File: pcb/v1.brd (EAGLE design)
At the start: 92 x 80 mm, 54 parts, among them U2 MMBT3904, U3 MMBT3904, U4 MMBT3904, U5 MMBT3904

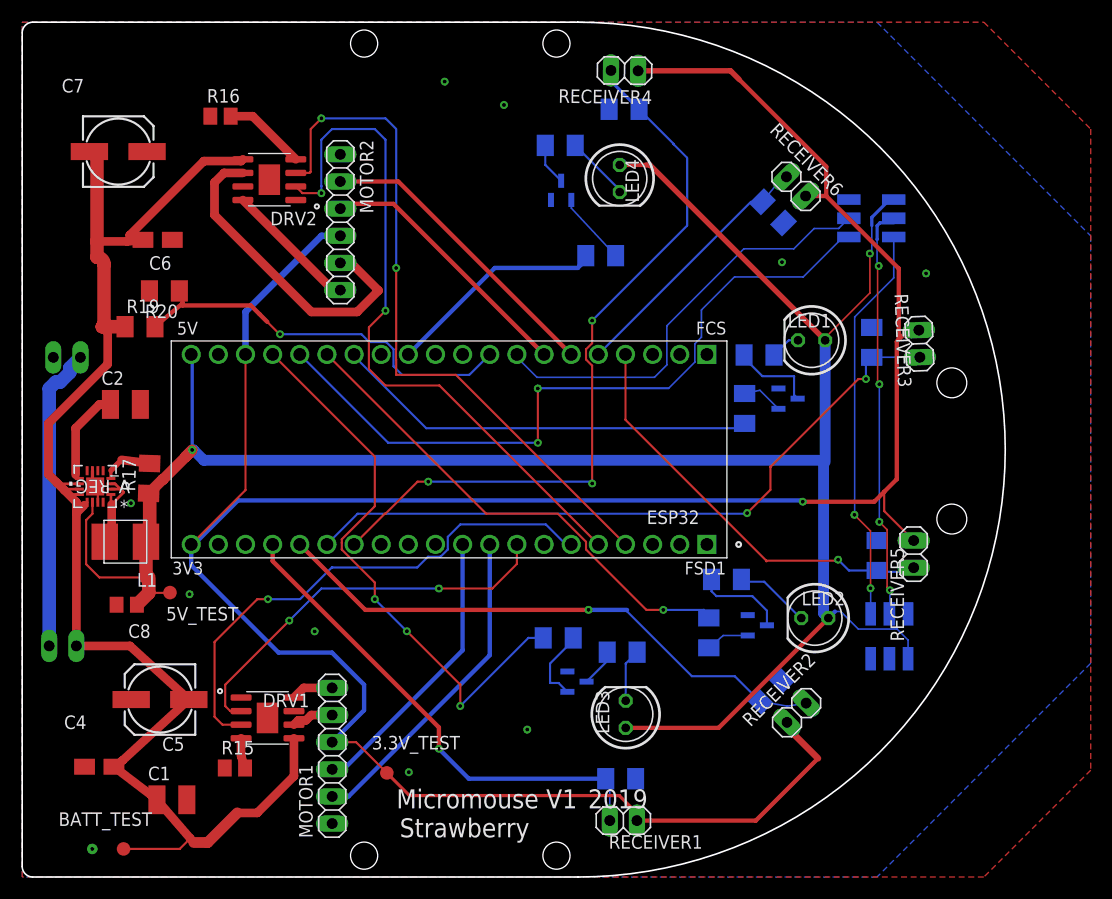
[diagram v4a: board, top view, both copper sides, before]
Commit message: Changed pin placement
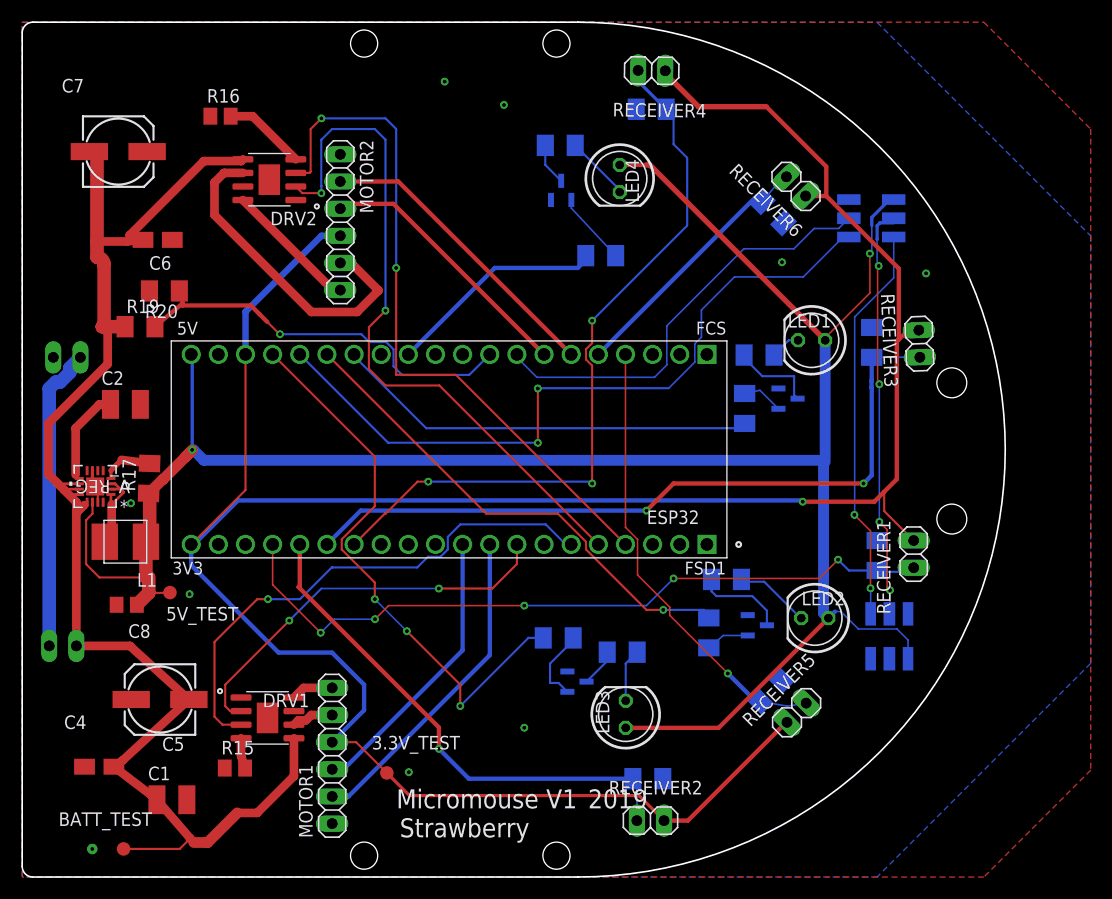
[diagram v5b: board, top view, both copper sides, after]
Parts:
- moved RECEIVER1 36.9 mm to (83.4, 30.2), turned to 270 degrees
- moved RECEIVER5 18.4 mm to (72.5, 15.4), turned to 45 degrees
- moved RECEIVER2 17.0 mm to (58.8, 5.28), turned to 180 degrees
- moved R12 2.54 mm to (58.9, 71.9)
- moved R9 2.54 mm to (58.5, 9.20)
- moved RECEIVER4 2.54 mm to (58.9, 75.5)
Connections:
- net REC1: now also R13.2; no longer R9.2
- net REC2: now also R9.2; no longer R10.2
- net REC5: now also R10.2; no longer R13.2
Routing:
- net REC1: track 46.4 -> 69.2 mm, vias 1 -> 5
- net 3.3V: track 253.0 -> 244.1 mm
- net REC2: track 53.6 -> 48.0 mm
- net REC3: track 64.9 -> 69.2 mm
- net REC5: track 39.3 -> 43.1 mm
- net REC4: track 70.6 -> 69.5 mm
- net REC6: track 24.6 -> 25.2 mm

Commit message: Flipped the back sensor resistors
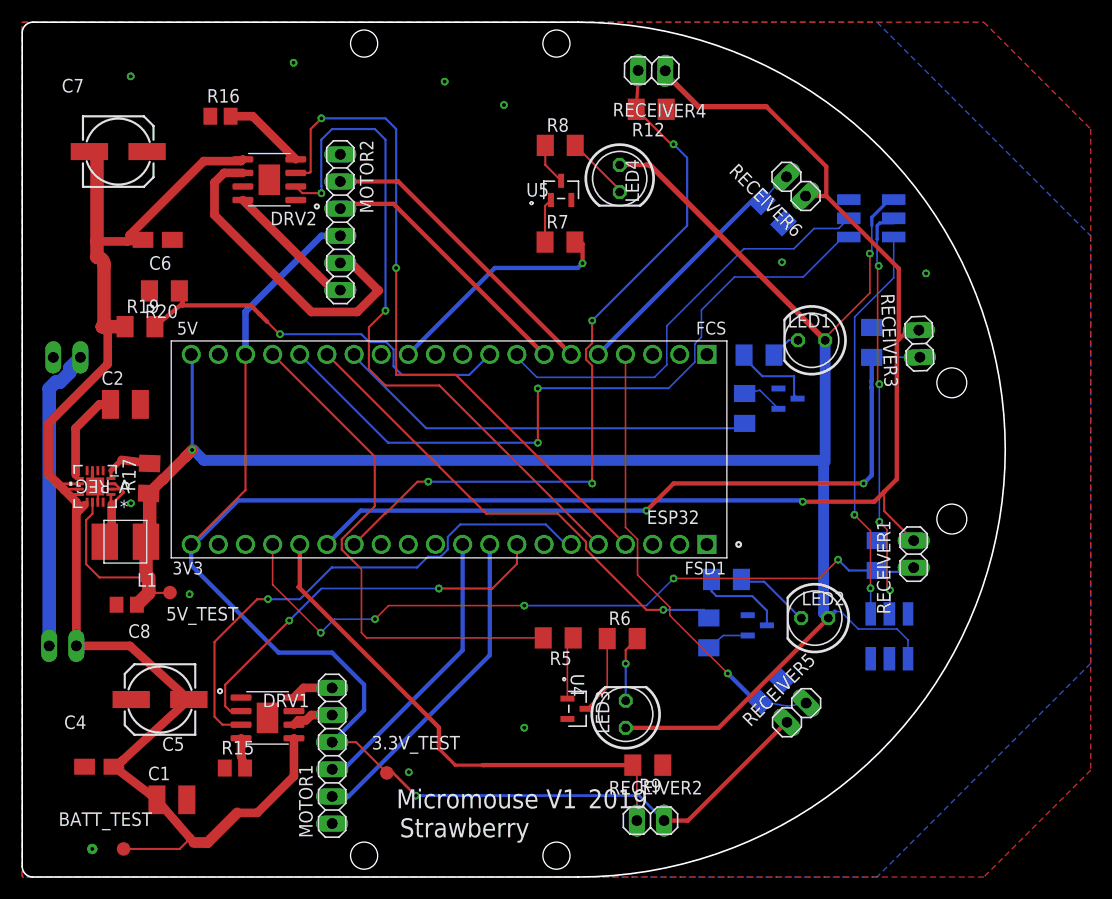
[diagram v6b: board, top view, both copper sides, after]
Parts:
- moved R7 4.02 mm to (50.3, 59.4), flipped to the top
- moved U4 2.54 mm to (52.0, 15.7), flipped to the top, turned to 270 degrees
- moved R6 1.27 mm to (56.2, 22.3), flipped to the top, turned to 0 degrees
- moved R9 1.27 mm to (58.5, 10.5), flipped to the top, turned to 180 degrees
- flipped R12 to the top
- flipped R5 to the top, turned to 180 degrees
- flipped R8 to the top, turned to 0 degrees
- flipped U5 to the top
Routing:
- net N$12: track 3.56 -> 7.47 mm
- net EM3: track 53.2 -> 49.3 mm, vias 3 -> 0
- net N$13: track 6.85 -> 4.18 mm
- net EM4: track 20.6 -> 22.4 mm, vias 0 -> 1
- net N$11: track 4.99 -> 6.26 mm, vias 0 -> 1
- net N$10: track 7.08 -> 5.91 mm
- net 5V: track 205.4 -> 204.3 mm
- net REC2: track 48.0 -> 48.9 mm, vias 1 -> 0
- net REC4: track 69.5 -> 69.7 mm, vias 3 -> 4
- net 3.3V: vias 1 -> 2

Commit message: Evened out the holes to make pcb look nicer
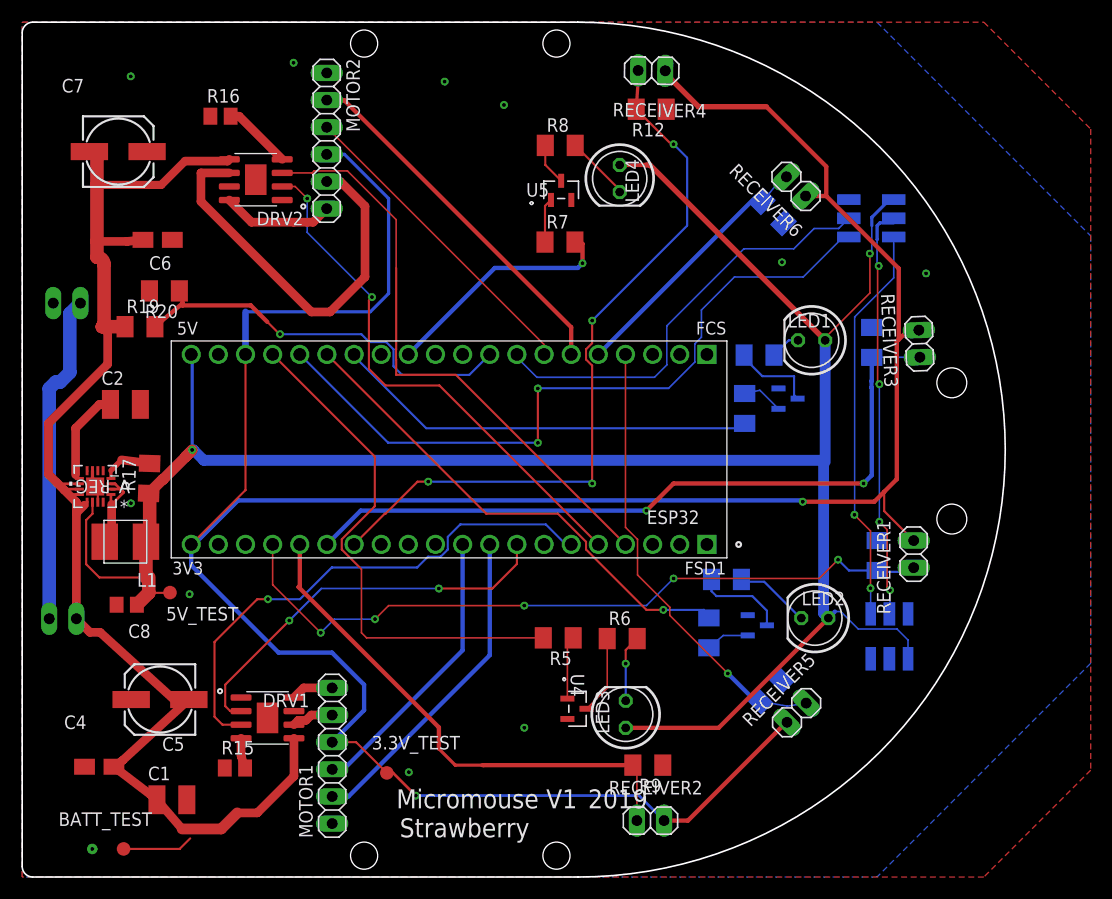
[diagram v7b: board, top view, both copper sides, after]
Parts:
- moved MOTOR2 7.73 mm to (28.5, 68.9)
- moved BATT2 5.08 mm to (4.18, 53.7)
- moved BATT1 2.54 mm to (3.80, 24.2)
- moved DRV2 1.27 mm to (21.9, 65.3)
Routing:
- net 3.3V: track 244.1 -> 262.8 mm
- net PWM1B: track 64.9 -> 49.7 mm
- net PWM1A: track 65.3 -> 55.2 mm, vias 2 -> 0
- net N$19: track 30.7 -> 37.5 mm
- net EN1A: track 28.3 -> 34.2 mm
- net EN1B: track 25.1 -> 29.7 mm
- net BATT_POWER: track 133.0 -> 128.9 mm
- net N$1: track 28.5 -> 31.0 mm
- net N$18: track 12.6 -> 10.5 mm
- net N$20: track 7.77 -> 6.50 mm

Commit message: Changed the voltage regulator and updated the pcb
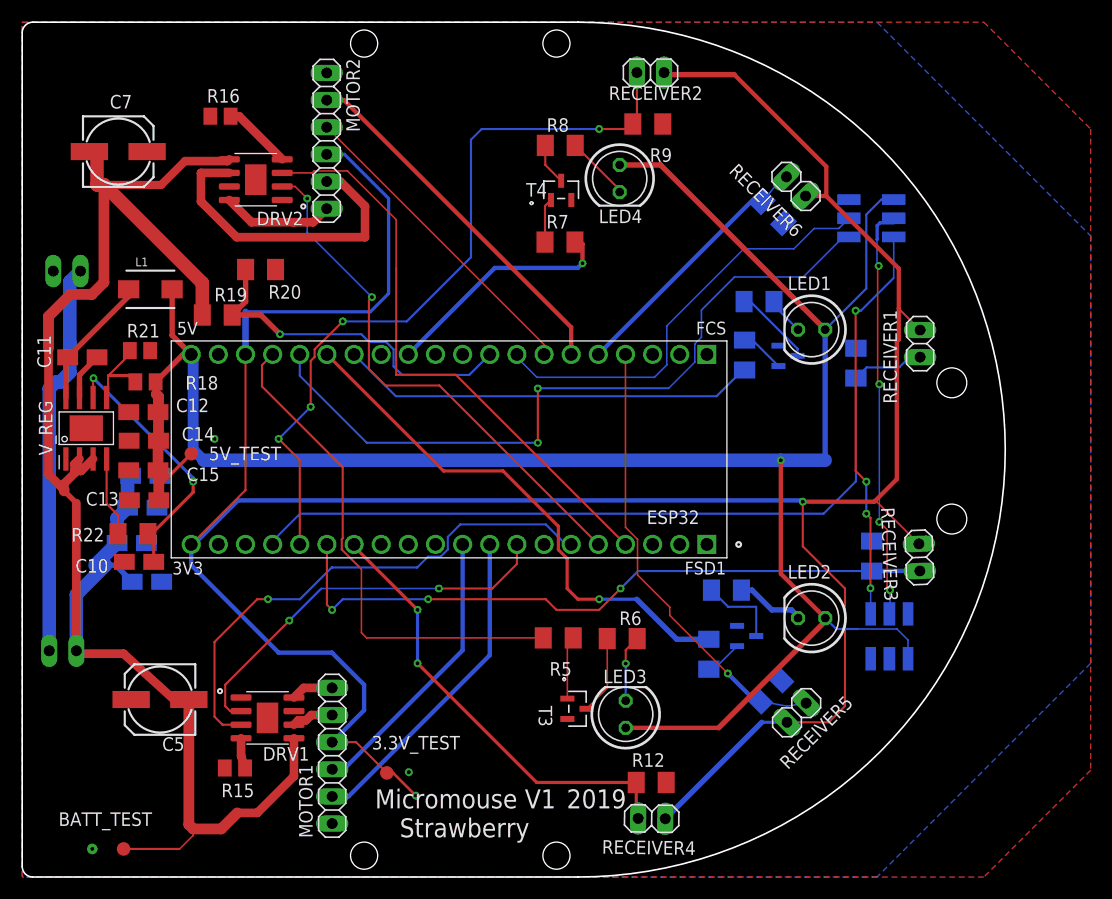
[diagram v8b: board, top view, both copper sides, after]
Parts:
- removed C1: 10uF, rcl:C1210
- removed C2: 3.3nf, rcl:C1210
- removed C8: 22uF, rcl:C0805
- removed R17: 100, rcl:M1206
- removed U2, U3: MMBT3904, transistors:SOT23
- added C10, C11: .1uF, rcl:A/3216-18R
- added C12, C13, C14, C15, C3: 10uF, rcl:A/3216-18R
- added C9: 220nF, rcl:A/3216-18R
- added R18: 100k, rcl:M2012
- added R21: 24.9k, rcl:M2012
- added R22: 100k, rcl:M1206
- added T1, T2: MMBT3904, transistors:SOT23
- L1: value 2.2uH -> 8.2uH; device XFL4020:XFL4020 -> rc-master-smd:PM1812
- V_REG: value TPS62143RGTT -> LMR33620; device TPS61243RGTT:RGT16_1P7X1P7 -> LMR33620:SO-8_POWERPAD
- moved RECEIVER2 70.0 mm to (58.8, 75.3)
- moved RECEIVER4 70.0 mm to (58.9, 5.47)
- moved R12 63.0 mm to (58.9, 8.85)
- moved R9 60.0 mm to (58.5, 70.5)
- moved C6 32.0 mm to (11.7, 27.6), flipped to the bottom, turned to 0 degrees
- moved L1 23.7 mm to (12.0, 55.0)
- moved C4 21.2 mm to (10.3, 31.3), flipped to the bottom
- moved R11 20.0 mm to (79.5, 30.0)
- moved RECEIVER3 20.0 mm to (84.0, 29.9)
- moved RECEIVER1 19.7 mm to (84.0, 49.9)
- moved R13 18.1 mm to (78.0, 48.1)
- moved 5V_TEST 13.2 mm to (15.8, 39.6)
- moved R20 9.22 mm to (22.3, 56.9), turned to 0 degrees
- moved R19 7.31 mm to (18.3, 52.6)
- moved V_REG 5.51 mm to (6.00, 42.0), turned to 0 degrees
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- renumbered U4 to T3, U5 to T4
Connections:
- removed net N$2: C2.1, V_REG.9
- removed net N$21: L1.P$2, V_REG.1, V_REG.2, V_REG.3
- removed net N$22: R17.2, V_REG.4
- removed net N$4: R3.1, U3.1
- new net N$23: R18.1, R21.2, V_REG.5
- new net N$25: C11.+, V_REG.7
- new net N$26: C11.-, L1.2, V_REG.8
- new net PG: R22.1, V_REG.4
- new net T1: R3.1, T1.1
- new net VCC: C10.+, R22.2, V_REG.6
- net 5V: now also C12.+, C13.+, C14.+, C15.+, L1.1, R18.2; no longer C8.1, L1.P$1, R17.1, V_REG.14
- net BATT_POWER: now also C3.+, C9.+, V_REG.2, V_REG.3; no longer C1.1, V_REG.10, V_REG.11, V_REG.12, V_REG.13
- net GND: now also C10.-, C12.-, C13.-, C14.-, C15.-, C3.-, C9.-, R21.1, T1.2, T2.2, V_REG.1, V_REG.POWERPAD_BOTTOM, V_REG.POWERPAD_TOP; no longer C1.2, C2.2, C8.2, U2.2, U3.2, V_REG.15, V_REG.16, V_REG.17, V_REG.5, V_REG.6, V_REG.7, V_REG.8
- net N$5: now also T2.1; no longer U2.1
- net N$7: now also T2.3; no longer U2.3
- net N$9: now also T1.3; no longer U3.3
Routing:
- net BATT_POWER: track 128.9 -> 157.7 mm
- net REC4: track 69.7 -> 42.1 mm, vias 4 -> 2
- net VCC: track 0.00 -> 25.1 mm, vias 0 -> 2
- net REC2: track 48.9 -> 70.4 mm, vias 0 -> 4
- net N$26: track 0.00 -> 12.6 mm, vias 1 -> 0
- net 3.3V: track 262.8 -> 272.6 mm
- net N$2: track 9.03 -> 0.00 mm, vias 0 -> 1
- net N$21: track 8.75 -> 0.00 mm
- net N$23: track 0.00 -> 8.05 mm, vias 1 -> 0
- net N$19: track 37.5 -> 29.5 mm
- net PG: track 0.00 -> 7.44 mm
- net V_SENSE: track 39.2 -> 32.9 mm
- net N$1: track 31.0 -> 37.0 mm
- net REC3: track 69.2 -> 63.7 mm, vias 2 -> 3
- net N$22: track 4.80 -> 0.00 mm
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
